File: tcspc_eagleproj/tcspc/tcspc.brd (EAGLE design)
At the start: 120 x 74.9 mm, 86 parts, among them U1 THS788, U2 MCP4725, U3 ADCMP582, U4 LT6003_SOT23-5, U5 LT6003_SOT23-5, X1 SMA

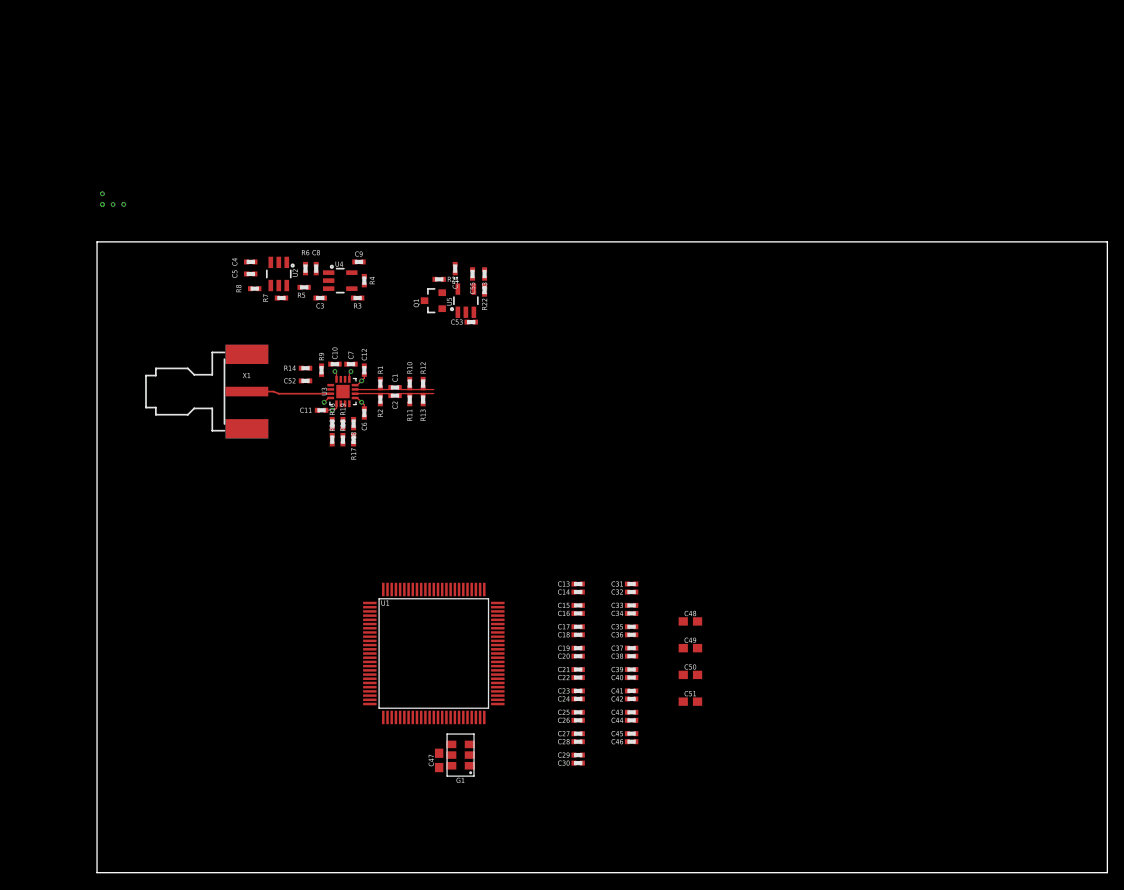
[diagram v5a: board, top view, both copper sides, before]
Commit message: turned the frontend into a useful designblock, ready to be pased all over the tcspc board
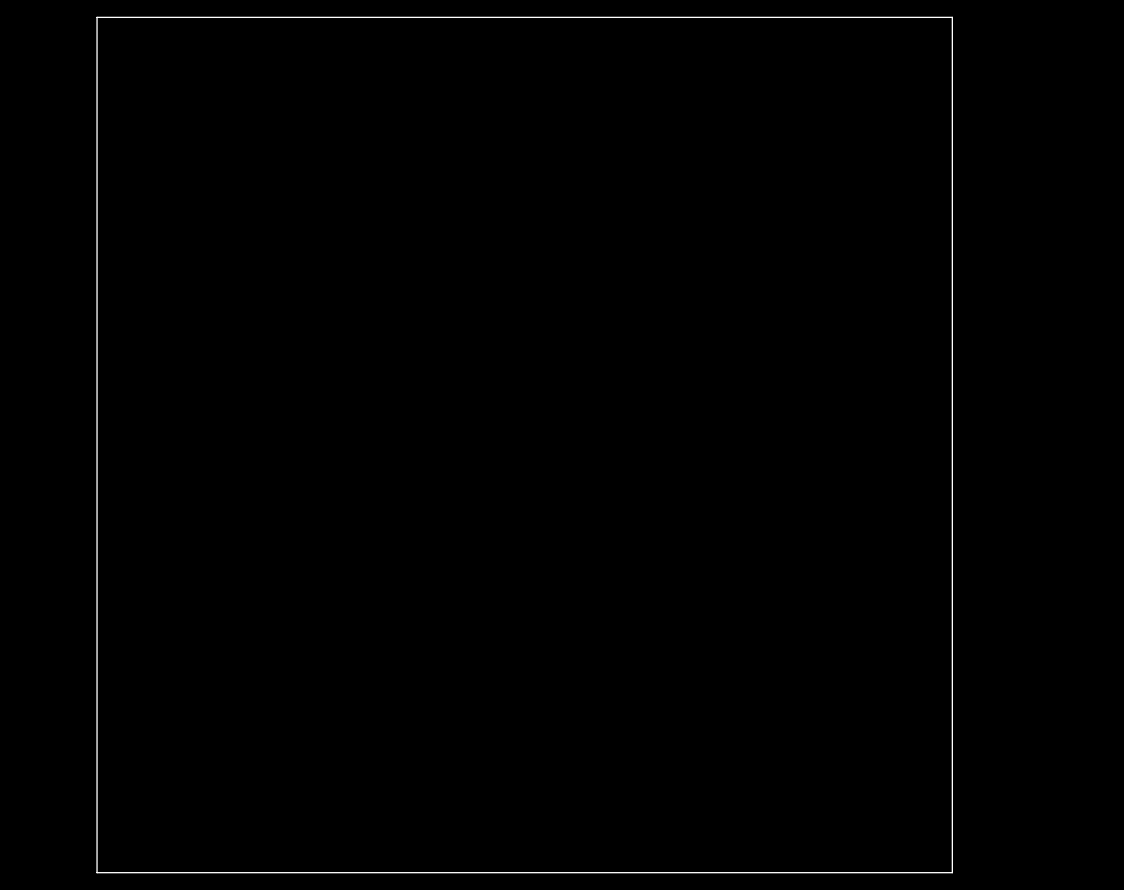
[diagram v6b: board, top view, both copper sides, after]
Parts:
- removed C1, C2: 10pF, tcspc_lib:0402
- removed C10, C11, C12, C13, C15, C17, C19, C21, C23, C25, C27, C29, C3, C31, C33, C35, C37, C39, C4, C41, C43, C45, C53, C54, C55, C6, C7, C8, C9: .1uF, tcspc_lib:0402
- removed C14, C16, C18, C20, C22, C24, C26, C28, C30, C32, C34, C36, C38, C40, C42, C44, C46, C52: 10nF, tcspc_lib:0402
- removed C47: .1uF, tcspc_lib:0603
- removed C48, C49, C50, C51: 1uF, tcspc_lib:0603
- removed C5: 10uF, tcspc_lib:0402
- removed G1: 200MHz, tcspc_lib:SIT5021_5X3.2
- removed Q1: (no value), jack_semi:SOT23-3
- removed R1, R2: 50, tcspc_lib:0402
- removed R10, R11, R12, R13: (no value), tcspc_lib:0402
- removed R14, R6, R9: 0, tcspc_lib:0402
- removed R15: 210, tcspc_lib:0402
- removed R16: 100, tcspc_lib:0402
- removed R17, R18, R19, R20, R21, R22, R23: DNP, tcspc_lib:0402
- removed R3, R4, R5: 1k, tcspc_lib:0402
- removed R7, R8: 2.2k, tcspc_lib:0402
- removed U1: THS788, tcspc_lib:S-QFP-G100
- removed U2: MCP4725, tcspc_lib:SOT23-6
- removed U3: ADCMP582, tcspc_lib:QFN50P300X300X80-16N
- removed U4, U5: LT6003_SOT23-5, tcspc_lib:SOT23-5
- removed X1: SMA, tcspc_lib:J502-ND-142-0701-881/886
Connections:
- removed net !TMU_DOUT_A: U1.79
- removed net !TMU_IN_A: U1.66
- removed net !TMU_IN_B: U1.63
- removed net !TMU_IN_C: U1.10
- removed net !TMU_IN_D: U1.13
- removed net GND: C10.2, C11.2, C12.2, C13.2, C14.2, C15.2, C16.2, C17.2, C18.2, C19.2, C20.2, C21.2, C22.2, C23.2, C24.2, C25.2, C26.2, C27.2, C28.2, C29.2, C3.2, C30.2, C31.2, C32.2, C33.2, C34.2, C35.2, C36.2, C37.2, C38.2, C39.2, C4.2, C40.2, C41.2, C42.2, C43.2, C44.2, C45.2, C46.2, C47.2, C48.2, C49.2, C5.2, C50.2, C51.2, C52.1, C53.2, C54.2, C55.2, C6.2, C7.1, C8.2, C9.2, G1.3, R1.2, R12.2, R13.2, R15.2, R18.2, R2.2, R20.2, R5.2, R9.1, U1.1, U1.11, U1.12, U1.2, U1.21, U1.25, U1.32, U1.35, U1.37, U1.39, U1.42, U1.55, U1.64, U1.65, U1.74, U1.75, U1.82, U1.84, U1.85, U1.87, U1.89, U1.92, U1.94, U2.2, U2.6, U3.15, U3.4, U5.3, X1.G@1, X1.G@2, X1.G@3, X1.G@4
- removed net N$1: G1.5, U1.20
- removed net N$10: U1.52
- removed net N$11: U1.53
- removed net N$12: R3.1, R4.2, U4.4
- removed net N$13: R14.1, R3.2, U4.1
- removed net N$14: U1.51
- removed net N$15: U1.33
- removed net N$16: U1.34
- removed net N$17: U1.41
- removed net N$18: U3.3, X1.1
- removed net N$19: R7.2, U2.5
- removed net N$2: G1.4, U1.19
- removed net N$20: R8.2, U2.4
- removed net N$21: U1.30
- removed net N$22: U1.29
- removed net N$23: U1.95
- removed net N$24: U1.96
- removed net N$25: U1.46
- removed net N$26: U1.47
- removed net N$27: U1.81
- removed net N$28: U1.80
- removed net N$29: U1.44
- removed net N$3: C2.1, R2.1, U3.10
- removed net N$30: U1.45
- removed net N$31: U1.28
- removed net N$32: U1.27
- removed net N$33: U1.97
- removed net N$34: U1.98
- removed net N$35: U1.48
- removed net N$36: U1.49
- removed net N$37: C52.2, R14.2, U3.2
- removed net N$38: R17.2, R18.1, U3.8
- removed net N$39: R15.1, R19.2, U3.7
- removed net N$4: C1.2, R10.2, R12.1
- removed net N$41: R16.2, R20.1, U3.6
- removed net N$42: Q1.3, U3.14
- removed net N$43: Q1.1, U5.1
- removed net N$45: C55.1, R22.2, R23.1, U5.4
- removed net N$46: R22.1
- removed net N$47: Q1.2, R21.1, R23.2
- removed net N$5: C2.2, R11.2, R13.1
- removed net N$6: C1.1, R1.1, U3.11
- removed net N$7: R9.2, U3.1
- removed net N$8: R6.1, U2.1
- removed net N$9: C3.1, R5.1, R6.2, U4.3
- removed net PP_N3V3_ANALOG: C53.1, C7.2, C8.1, R21.2, U3.13, U4.2, U5.2
- removed net PP_P3V3: C13.1, C14.1, C15.1, C16.1, C17.1, C18.1, C19.1, C20.1, C21.1, C22.1, C23.1, C24.1, C25.1, C26.1, C27.1, C28.1, C29.1, C30.1, C31.1, C32.1, C33.1, C34.1, C35.1, C36.1, C37.1, C38.1, C39.1, C40.1, C41.1, C42.1, C43.1, C44.1, C45.1, C46.1, C47.1, C48.1, C49.1, C50.1, C51.1, G1.6, U1.16, U1.22, U1.23, U1.24, U1.31, U1.36, U1.38, U1.40, U1.43, U1.58, U1.60, U1.69, U1.7, U1.77, U1.83, U1.86, U1.88, U1.90, U1.91, U1.93, U1.99
- removed net PP_P3V3_ANALOG: C10.1, C11.1, C4.1, C5.1, C54.1, C6.1, C9.1, R4.1, R7.1, R8.1, U2.3, U3.16, U3.5, U4.5, U5.5
- removed net PP_P3V3_DIGITAL: C12.1, R10.1, R11.1, R16.1, R17.1, R19.1, U3.12, U3.9
- removed net TMU_DOUT_A: U1.78
- removed net TMU_IN_A: U1.68
- removed net TMU_IN_B: U1.61
- removed net TMU_IN_C: U1.8
- removed net TMU_IN_D: U1.15
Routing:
- net N$18: track 10.0 -> 0.00 mm
- net N$5: track 4.63 -> 0.00 mm
- net N$4: track 4.63 -> 0.00 mm
- net N$3: track 4.56 -> 0.00 mm
- net N$6: track 4.56 -> 0.00 mm
- net PP_P3V3_ANALOG: track 4.53 -> 0.00 mm, vias 3 -> 0
- net PP_P3V3_DIGITAL: track 1.89 -> 0.00 mm, vias 1 -> 0
- net GND: track 0.99 -> 0.00 mm, vias 2 -> 0
- net PP_N3V3_ANALOG: track 0.74 -> 0.00 mm, vias 2 -> 0
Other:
- board size 120 x 74.9 mm -> 101.6 x 101.6 mm

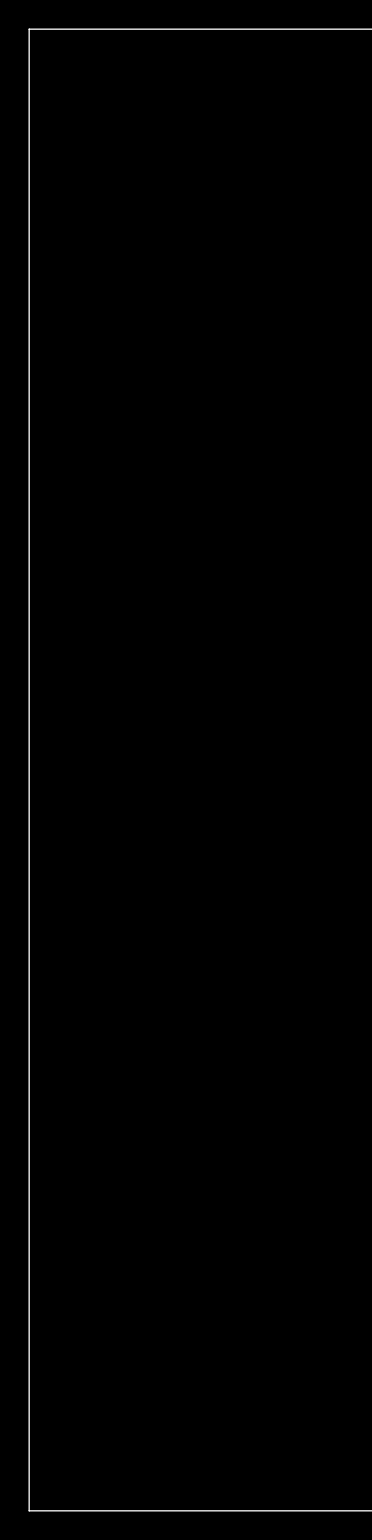
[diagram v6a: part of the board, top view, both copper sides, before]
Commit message: small tweaks to the dbl so that I could start putting four of them onto the main board, and then I did just that.
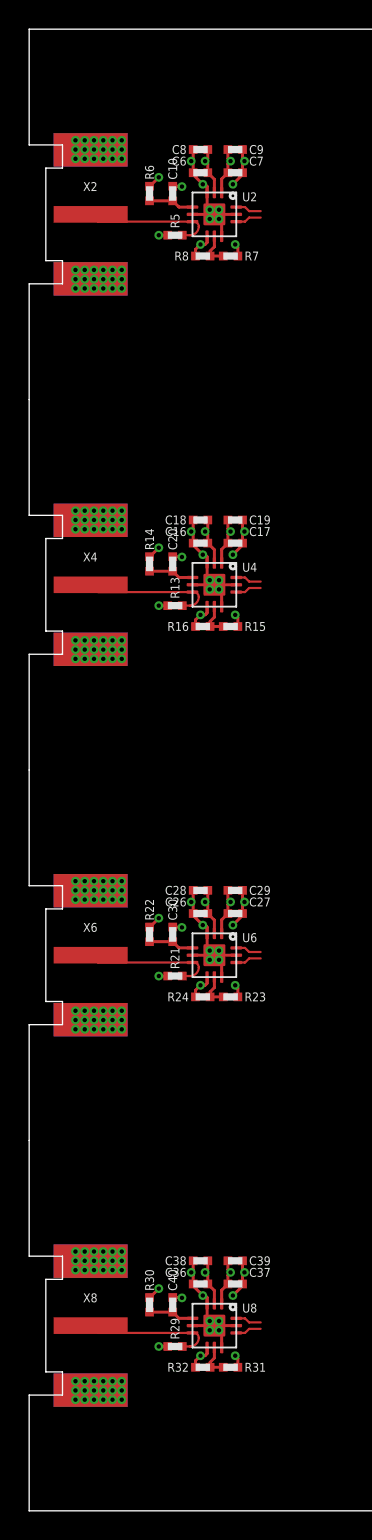
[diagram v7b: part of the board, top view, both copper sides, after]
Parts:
- added C10, C18, C19, C20, C28, C29, C30, C38, C39, C40, C8, C9: 100nF, tcspc_lib:0402
- added C16, C17, C26, C27, C36, C37, C6, C7: 10nF, tcspc_lib:0402
- added R13, R21, R29, R5: 50, tcspc_lib:0402
- added R14, R22, R30, R6: 1k, tcspc_lib:0402
- added R15, R23, R31, R7: 90.2k, tcspc_lib:0402
- added R16, R24, R32, R8: 55k, tcspc_lib:0402
- added U2, U4, U6, U8: AD8465, tcspc_lib:LFCSP-12
- added X2, X4, X6, X8: SMA, tcspc_lib:J502-ND-142-0701-881/886
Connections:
- new net CHA_HYS_SET: R7.1
- new net CHA_LE/HYS: R7.2, R8.1, U2.8
- new net CHA_OUT_N: U2.10
- new net CHA_OUT_P: U2.12
- new net CHA_SIG_IN: R5.1, U2.6, X2.1
- new net CHA_THRESH: C10.1, R6.2, U2.4
- new net CHA_THRESH_SET: R6.1
- new net CHB_HYS_SET: R15.1
- new net CHB_LE/HYS: R15.2, R16.1, U4.8
- new net CHB_OUT_N: U4.10
- new net CHB_OUT_P: U4.12
- new net CHB_SIG_IN: R13.1, U4.6, X4.1
- new net CHB_THRESH: C20.1, R14.2, U4.4
- new net CHB_THRESH_SET: R14.1
- new net CHC_HYS_SET: R23.1
- new net CHC_LE/HYS: R23.2, R24.1, U6.8
- new net CHC_OUT_N: U6.10
- new net CHC_OUT_P: U6.12
- new net CHC_SIG_IN: R21.1, U6.6, X6.1
- new net CHC_THRESH: C30.1, R22.2, U6.4
- new net CHC_THRESH_SET: R22.1
- new net CHD_HYS_SET: R31.1
- new net CHD_LE/HYS: R31.2, R32.1, U8.8
- new net CHD_OUT_N: U8.10
- new net CHD_OUT_P: U8.12
- new net CHD_SIG_IN: R29.1, U8.6, X8.1
- new net CHD_THRESH: C40.1, R30.2, U8.4
- new net CHD_THRESH_SET: R30.1
- new net GND: C10.2, C16.2, C17.2, C18.2, C19.2, C20.2, C26.2, C27.2, C28.2, C29.2, C30.2, C36.2, C37.2, C38.2, C39.2, C40.2, C6.2, C7.2, C8.2, C9.2, R13.2, R16.2, R21.2, R24.2, R29.2, R32.2, R5.2, R8.2, U2.11, U2.3, U2.5, U2.7, U2.9, U2.EPAD, U4.11, U4.3, U4.5, U4.7, U4.9, U4.EPAD, U6.11, U6.3, U6.5, U6.7, U6.9, U6.EPAD, U8.11, U8.3, U8.5, U8.7, U8.9, U8.EPAD, X2.G@1, X2.G@2, X2.G@3, X2.G@4, X4.G@1, X4.G@2, X4.G@3, X4.G@4, X6.G@1, X6.G@2, X6.G@3, X6.G@4, X8.G@1, X8.G@2, X8.G@3, X8.G@4
- new net PP_P3V3_ANALOG: C16.1, C18.1, C26.1, C28.1, C36.1, C38.1, C6.1, C8.1, U2.2, U4.2, U6.2, U8.2
- new net PP_P3V3_DIGITAL: C17.1, C19.1, C27.1, C29.1, C37.1, C39.1, C7.1, C9.1, U2.1, U4.1, U6.1, U8.1
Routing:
- net GND: track 0.00 -> 63.4 mm, vias 0 -> 188
- net PP_P3V3_ANALOG: track 0.00 -> 13.1 mm, vias 0 -> 4
- net PP_P3V3_DIGITAL: track 0.00 -> 13.1 mm, vias 0 -> 4
- net CHA_SIG_IN: track 0.00 -> 9.13 mm
- net CHD_SIG_IN: track 0.00 -> 9.13 mm
- net CHC_SIG_IN: track 0.00 -> 9.13 mm
- net CHB_SIG_IN: track 0.00 -> 9.13 mm
- net CHD_THRESH: track 0.00 -> 3.12 mm
- net CHC_THRESH: track 0.00 -> 3.12 mm
- net CHB_THRESH: track 0.00 -> 3.12 mm
- net CHA_THRESH: track 0.00 -> 3.12 mm
- net CHA_LE/HYS: track 0.00 -> 2.38 mm
- net CHC_LE/HYS: track 0.00 -> 2.38 mm
- net CHB_LE/HYS: track 0.00 -> 2.38 mm
- net CHD_LE/HYS: track 0.00 -> 2.38 mm
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- added copper zone on layer 2, net GND
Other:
- outline, holes or cut-outs redrawn

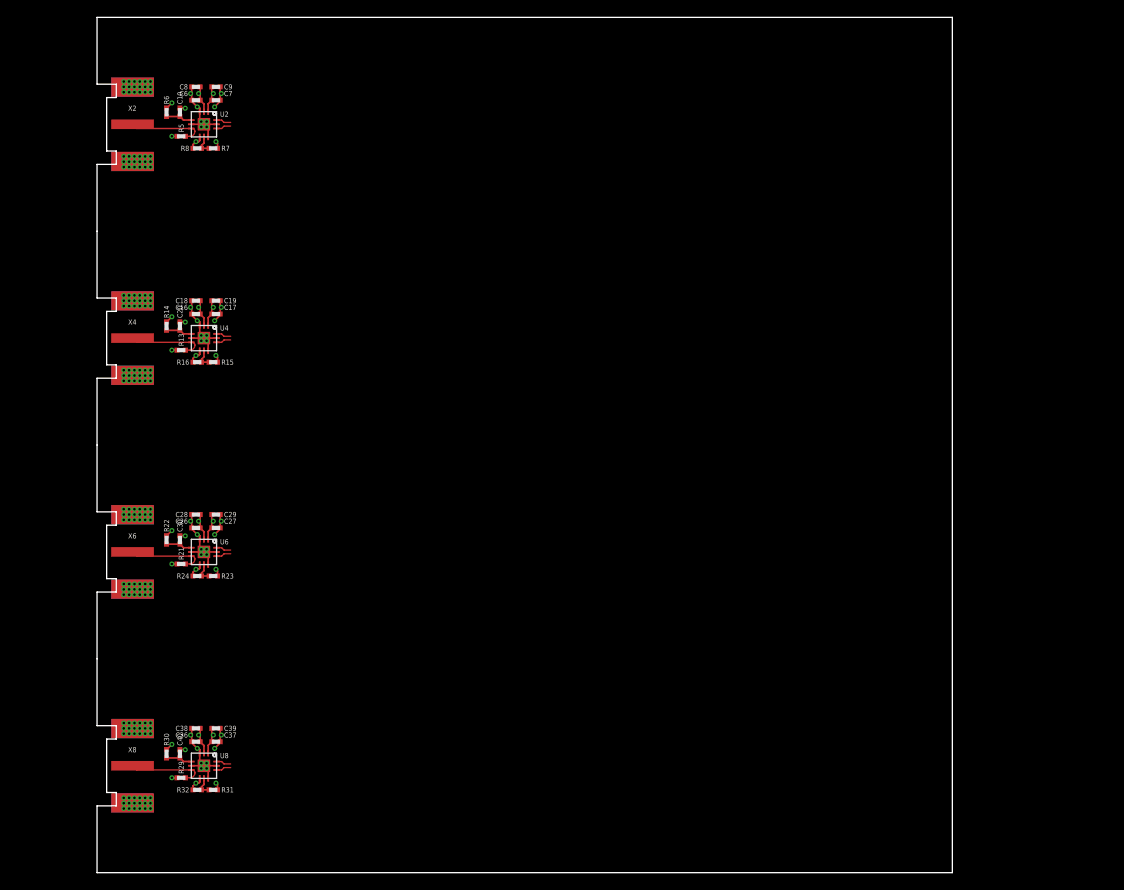
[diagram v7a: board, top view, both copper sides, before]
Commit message: created an FPGA device in the library, stuck it on the board and hooked up the various power pins to their nets. I also added the linear postregs and DAC to the schematic, and did some power calcs.
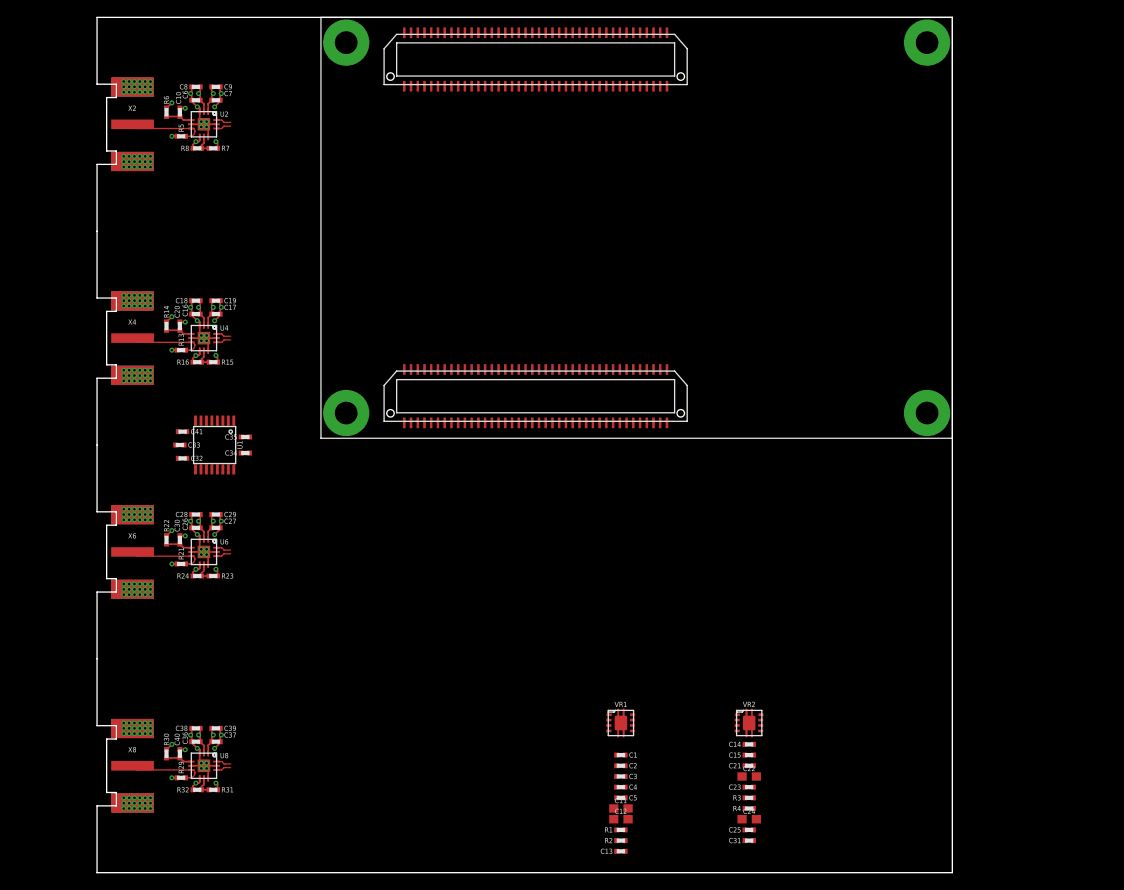
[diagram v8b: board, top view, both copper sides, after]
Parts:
- added C1, C2, C21, C25, C33, C34: 100nF, tcspc_lib:0402
- added C11, C12, C22, C24: 10uF, tcspc_lib:0603
- added C13, C14, C15, C23, C3, C31, C4, C5: 10nF, tcspc_lib:0402
- added C32, C35, C41: 10uF, tcspc_lib:0402
- added FPGA1: XEM7310, tcspc_lib:XEM7310
- added R1, R3: 17.8k, tcspc_lib:0402
- added R2, R4: 10k, tcspc_lib:0402
- added U1: AD53X8, tcspc_lib:TSSOP-16
- added VR1, VR2: (no value), tcspc_lib:VSON
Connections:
- new net DAC_!LDAC!: U1.1
- new net DAC_!SYNC!: U1.2
- new net DAC_DIN: U1.15
- new net DAC_SCLK: U1.16
- new net FPGA_SYS_CLK_MC1: FPGA1.MC1.8
- new net FPGA_SYS_CLK_MC2: FPGA1.MC2.11
- new net FPGA_TCK: FPGA1.MC2.5
- new net FPGA_TDI: FPGA1.MC2.9
- new net FPGA_TDO: FPGA1.MC2.8
- new net FPGA_TMS: FPGA1.MC2.7
- new net FPGA_VCCO_MC1: FPGA1.MC1.36, FPGA1.MC1.56
- new net FPGA_VCCO_MC2: FPGA1.MC2.35, FPGA1.MC2.55
- new net FPGA_XADC_VN: FPGA1.MC1.10
- new net FPGA_XADC_VP: FPGA1.MC1.12
- new net N$1: C1.1, C11.1, C13.1, VR1.5, VR1.8
- new net N$10: C23.2, R3.2, R4.1, VR2.2
- new net N$11: U1.6
- new net N$12: U1.7
- new net N$13: U1.10
- new net N$14: U1.11
- new net N$15: U1.12
- new net N$16: U1.13
- new net N$2: U1.4
- new net N$3: C4.2, R1.2, R2.1, VR1.2
- new net N$4: C3.1, VR1.6
- new net N$7: C15.1, C21.1, C22.1, VR2.5, VR2.8
- new net N$8: C14.1, VR2.6
- new net N$9: U1.5
- new net PP_P1V0_FPGA: FPGA1.MC1.4, FPGA1.MC1.6
- new net PP_P1V8_FPGA: FPGA1.MC1.7
- new net PP_P3V3_FPGA: FPGA1.MC1.11, FPGA1.MC1.13, FPGA1.MC1.9, FPGA1.MC2.2, FPGA1.MC2.4, FPGA1.MC2.6
- new net PP_VCCBATT_FPGA: FPGA1.MC2.3
- new net PP_VDCIN_FPGA: FPGA1.MC1.1, FPGA1.MC1.3, FPGA1.MC1.5
- net GND: now also C1.2, C11.2, C12.2, C13.2, C14.2, C15.2, C2.2, C21.2, C22.2, C24.2, C25.2, C3.2, C31.2, C32.2, C33.2, C34.2, C35.2, C41.2, C5.2, FPGA1.MC1.14, FPGA1.MC1.2, FPGA1.MC1.35, FPGA1.MC1.55, FPGA1.MC1.78, FPGA1.MC1.80, FPGA1.MC2.1, FPGA1.MC2.13, FPGA1.MC2.14, FPGA1.MC2.36, FPGA1.MC2.56, FPGA1.MC2.78, FPGA1.MC2.80, R2.2, R4.2, U1.14, VR1.4, VR1.TP, VR1.TP_A, VR1.TP_B, VR1.TP_C, VR1.TP_D, VR2.4, VR2.TP, VR2.TP_A, VR2.TP_B, VR2.TP_C, VR2.TP_D
- net PP_P3V3_ANALOG: now also C12.1, C2.1, C32.1, C33.1, C4.1, C41.1, C5.1, R1.1, U1.8, U1.9, VR1.1
- net PP_P3V3_DIGITAL: now also C23.1, C24.1, C25.1, C31.1, C34.1, C35.1, R3.1, U1.3, VR2.1
